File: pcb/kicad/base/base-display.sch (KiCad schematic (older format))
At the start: 3 parts

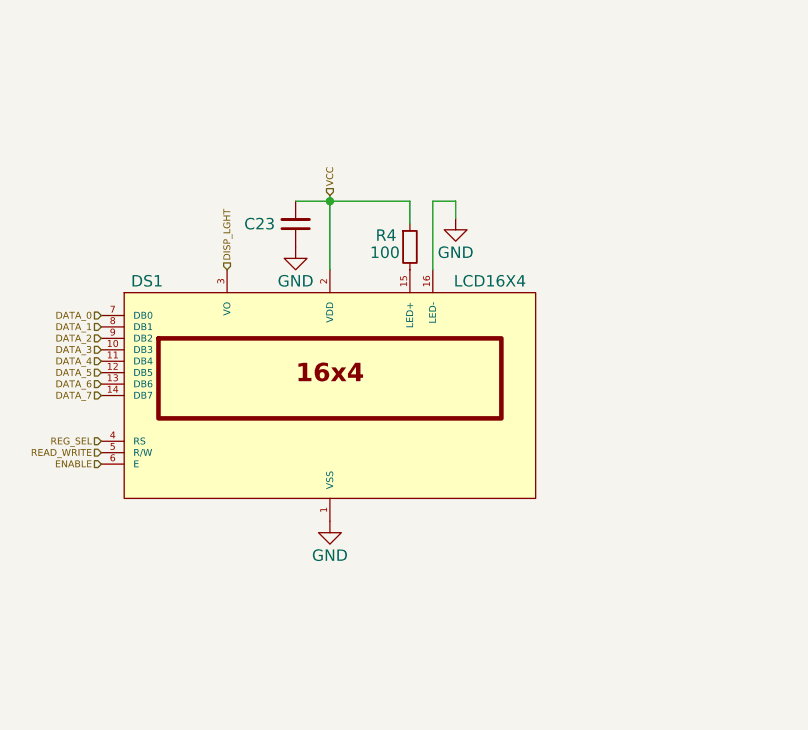
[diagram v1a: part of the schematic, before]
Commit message: Update display and XBee position
Display is now placed on top of uC to shrink total package dimensions
and the XBee has been moved to accompany this change. Net vias have
been fixed to fit Bay Area Circuits' design constraints.
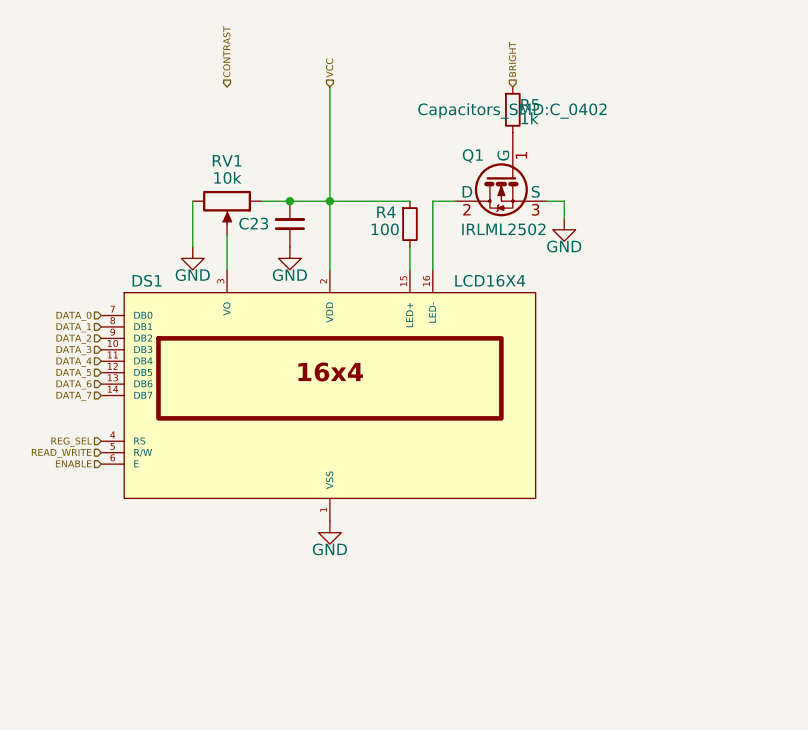
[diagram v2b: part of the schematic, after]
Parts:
- added Q1: IRLML2502, TO_SOT_Packages_SMD:SOT-23, symbol IRLB8721PBF
- added R5: 1k, Capacitors_SMD:C_0402, symbol R_Small
- added RV1: 10k, Potentiometers:Potentiometer_Trimmer_Bourns_3296W, symbol POT
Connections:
- net GND: now also Q1.3 (S), RV1.3; no longer DS1.16 (LED-)
- net VCC: now also RV1.1
- net DISP_LGHT: no longer names the net of DS1.3 (VO)
- net DISP_LGHT: now also RV1.2
- new net: DS1.16 (LED-), Q1.2 (D)
- new net: Q1.1 (G), R5.2
- new net BRIGHT: R5.1
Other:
- moved on the sheet: C23, R4
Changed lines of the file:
@@
 $EndComp
 $Comp
-L GND #PWR028
+L GND #PWR029
 U 1 1 58DBA50D
 P 5850 4050
-F 0 "#PWR028" H 5850 3800 50  0001 C CNN
-F 1 "GND" H 5850 3900 50  0000 C CNN
+F 0 "#PWR029" H 5850 3800 50  0001 C CNN
+F 1 "GND" H 5850 3925 50  0000 C CNN
 F 2 "" H 5850 4050 50  0001 C CNN
 F 3 "" H 5850 4050 50  0001 C CNN
@@
 Text HLabel 4850 3800 0    30   Input ~ 0
 ENABLE
-Text HLabel 5850 2625 1    30   Input ~ 0
+Text HLabel 5850 2150 1    30   Input ~ 0
 VCC
-Text HLabel 5400 2950 1    30   Input ~ 0
-DISP_LGHT
+Text HLabel 5400 2150 1    30   Input ~ 0
+CONTRAST
 $Comp
 L R_Small R4
 U 1 1 58DC9BBD
-P 6200 2850
-F 0 "R4" H 6050 2900 50  0000 L CNN
-F 1 "100" H 6025 2825 50  0000 L CNN
-F 2 "Capacitors_SMD:C_0402" H 6200 2850 50  0001 C CNN
-F 3 "" H 6200 2850 50  0001 C CNN
-	1    6200 2850
+P 6200 2750
+F 0 "R4" H 6050 2800 50  0000 L CNN
+F 1 "100" H 6025 2725 50  0000 L CNN
+F 2 "Capacitors_SMD:C_0402" H 6200 2750 50  0001 C CNN
+F 3 "" H 6200 2750 50  0001 C CNN
+	1    6200 2750
 	1    0    0    -1
 $EndComp
 $Comp
-L GND #PWR029
+L GND #PWR030
 U 1 1 58DCAC87
-P 6400 2725
-F 0 "#PWR029" H 6400 2475 50  0001 C CNN
-F 1 "GND" H 6400 2575 50  0000 C CNN
-F 2 "" H 6400 2725 50  0001 C CNN
-F 3 "" H 6400 2725 50  0001 C CNN
-	1    6400 2725
+P 6875 2725
+F 0 "#PWR030" H 6875 2475 50  0001 C CNN
+F 1 "GND" H 6875 2600 50  0000 C CNN
+F 2 "" H 6875 2725 50  0001 C CNN
+F 3 "" H 6875 2725 50  0001 C CNN
+	1    6875 2725
 	1    0    0    -1
 $EndComp
@@
 L C_Small C23
 U 1 1 58DCAD0E
-P 5700 2750
-F 0 "C23" H 5475 2750 50  0000 L CNN
-F 1 "C_Small" H 5710 2670 50  0001 L CNN
-F 2 "Capacitors_SMD:C_0402" H 5700 2750 50  0001 C CNN
-F 3 "" H 5700 2750 50  0001 C CNN
-	1    5700 2750
+P 5675 2750
+F 0 "C23" H 5450 2750 50  0000 L CNN
+F 1 "C_Small" H 5685 2670 50  0001 L CNN
+F 2 "Capacitors_SMD:C_0402" H 5675 2750 50  0001 C CNN
+F 3 "" H 5675 2750 50  0001 C CNN
+	1    5675 2750
 	1    0    0    1
 $EndComp
 $Comp
-L GND #PWR030
+L GND #PWR031
 U 1 1 58DCDD1C
-P 5700 2850
-F 0 "#PWR030" H 5700 2600 50  0001 C CNN
-F 1 "GND" H 5700 2700 50  0000 C CNN
-F 2 "" H 5700 2850 50  0001 C CNN
-F 3 "" H 5700 2850 50  0001 C CNN
-	1    5700 2850
+P 5675 2850
+F 0 "#PWR031" H 5675 2600 50  0001 C CNN
+F 1 "GND" H 5675 2725 50  0000 C CNN
+F 2 "" H 5675 2850 50  0001 C CNN
+F 3 "" H 5675 2850 50  0001 C CNN
+	1    5675 2850
 	1    0    0    -1
 $EndComp
-Wire Wire Line
-	6200 2650 6200 2750
 Wire Wire Line
 	6300 2950 6300 2650
@@
 	6300 2650 6400 2650
 Wire Wire Line
-	6400 2650 6400 2725
-Wire Wire Line
-	5850 2625 5850 2950
-Wire Wire Line
-	5700 2650 6200 2650
-Connection ~ 5850 2650
+	5850 2150 5850 2950
 Text Notes 7325 7500 0    60   ~ 0
 Base - Display
@@
 Text HLabel 4850 3500 0    30   Input ~ 0
 DATA_7
+$Comp
+L IRLB8721PBF Q1
+U 1 1 58E6ED14
+P 6600 2550
+F 0 "Q1" V 6500 2625 50  0000 L CNN
+F 1 "IRLML2502" V 6825 2350 50  0000 L CNN
+F 2 "TO_SOT_Packages_SMD:SOT-23" H 6850 2475 50  0001 L CIN
+F 3 "" H 6600 2550 50  0000 L CNN
+	1    6600 2550
+	0    -1   1    0
+$EndComp
+Wire Wire Line
+	6800 2650 6875 2650
+Wire Wire Line
+	6875 2650 6875 2725
+$Comp
+L R_Small R5
+U 1 1 58E6F3FD
+P 6650 2250
+F 0 "R5" H 6680 2270 50  0000 L CNN
+F 1 "1k" H 6680 2210 50  0000 L CNN
+F 2 "Capacitors_SMD:C_0402" H 6650 2250 50  0000 C CNN
+F 3 "" H 6650 2250 50  0000 C CNN
+	1    6650 2250
+	1    0    0    -1
+$EndComp
+Text HLabel 6650 2150 1    30   Input ~ 0
+BRIGHT
+Wire Wire Line
+	6200 2950 6200 2850
+Wire Wire Line
+	5550 2650 6200 2650
+Connection ~ 5850 2650
+$Comp
+L POT RV1
+U 1 1 58E926EF
+P 5400 2650
+F 0 "RV1" V 5225 2650 50  0000 C CNN
+F 1 "10k" V 5300 2650 50  0000 C CNN
+F 2 "Potentiometers:Potentiometer_Trimmer_Bourns_3296W" H 5400 2650 50  0001 C CNN
+F 3 "" H 5400 2650 50  0000 C CNN
+	1    5400 2650
+	0    1    1    0
+$EndComp
+Connection ~ 5675 2650
+Wire Wire Line
+	5400 2800 5400 2950
+$Comp
+L GND #PWR032
+U 1 1 58E927A3
+P 5250 2850
+F 0 "#PWR032" H 5250 2600 50  0001 C CNN
+F 1 "GND" H 5250 2725 50  0000 C CNN
+F 2 "" H 5250 2850 50  0001 C CNN
+F 3 "" H 5250 2850 50  0001 C CNN
+	1    5250 2850
+	1    0    0    -1
+$EndComp
+Wire Wire Line
+	5250 2850 5250 2650
 $EndSCHEMATC

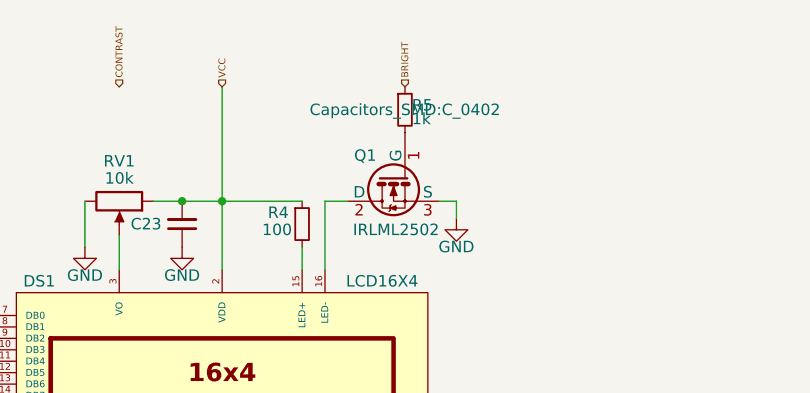
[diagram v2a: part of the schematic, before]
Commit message: Fix power and display routing with proper via size
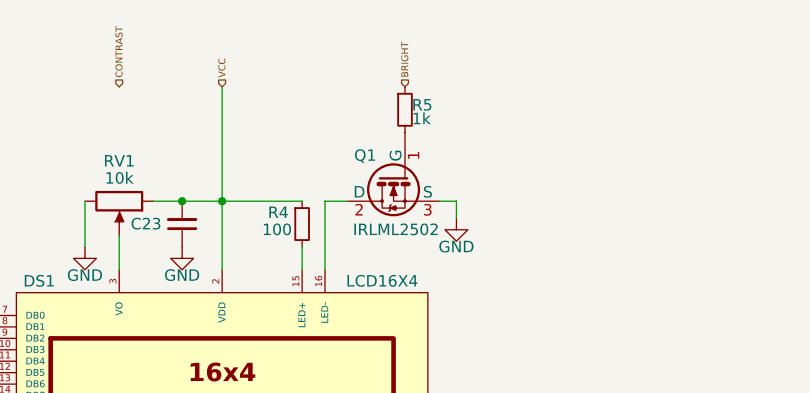
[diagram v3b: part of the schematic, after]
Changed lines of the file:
@@
 F 0 "R5" H 6680 2270 50  0000 L CNN
 F 1 "1k" H 6680 2210 50  0000 L CNN
-F 2 "Capacitors_SMD:C_0402" H 6650 2250 50  0000 C CNN
+F 2 "Capacitors_SMD:C_0402" H 6650 2250 50  0001 C CNN
 F 3 "" H 6650 2250 50  0000 C CNN
 	1    6650 2250

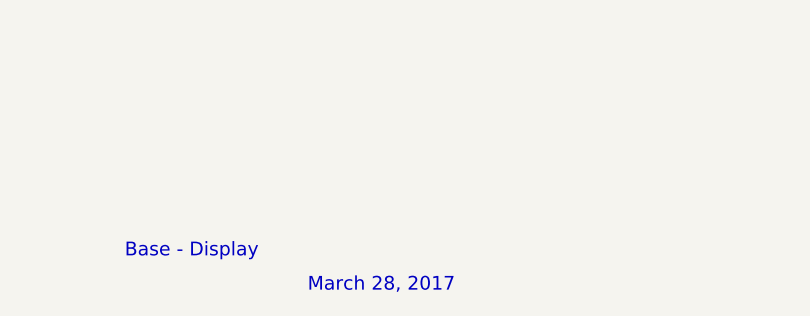
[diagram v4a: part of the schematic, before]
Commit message: Add ground stitch vias and silk identifiers
Base station layout is finished, and artwork has been generated.
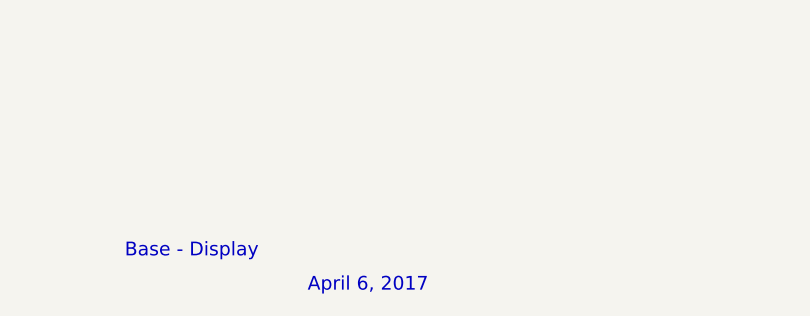
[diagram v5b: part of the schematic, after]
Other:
- note added: "April 6, 2017"
- note removed: "March 28, 2017"
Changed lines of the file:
@@
 Base - Display
 Text Notes 8125 7650 0    60   ~ 0
-March 28, 2017
+April 6, 2017
 Text Notes 10550 7650 0    60   ~ 0
 0.1

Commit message: Cleanup archive and pdfs
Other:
- note added: "LCD brightness to be\ncontrolled through PWM."
- note added: "Text contrast currently controlled\nwith potentiometer; potentially\nto be controlled with PWM."
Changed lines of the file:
@@
 Wire Wire Line
 	5250 2850 5250 2650
+Text Notes 6975 2200 0    60   ~ 0
+LCD brightness to be\ncontrolled through PWM.
+Text Notes 4950 2175 2    60   ~ 0
+Text contrast currently controlled\nwith potentiometer; potentially\nto be controlled with PWM.
 $EndSCHEMATC

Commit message: Update pad sizes on pin headers and XBee
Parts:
- DS1: footprint CFAH1604A -> Displays:CFAH1604A
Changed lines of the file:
@@
 F 0 "DS1" H 5050 4000 50  0000 C CNN
 F 1 "LCD16X4" H 6550 4000 50  0000 C CNN
-F 2 "CFAH1604A" H 5850 3450 50  0001 C CIN
+F 2 "Displays:CFAH1604A" H 5850 3450 50  0001 C CIN
 F 3 "" H 5850 3500 50  0001 C CNN
 	1    5850 3500
